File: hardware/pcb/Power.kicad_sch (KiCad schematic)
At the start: 12 parts, among them J2 USB_B_Micro, SW1 CSS-1210TB, U1 XC6808A4D28R-G, U3 NCP160AMX330TBG, U5 RN4989

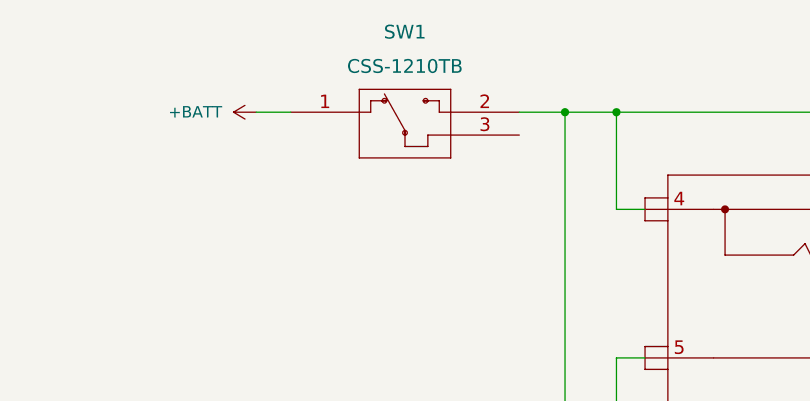
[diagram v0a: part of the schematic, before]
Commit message: Bump KiCad version to 7
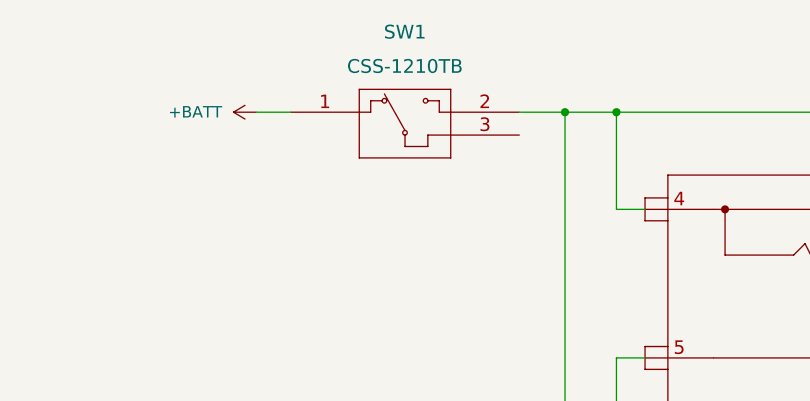
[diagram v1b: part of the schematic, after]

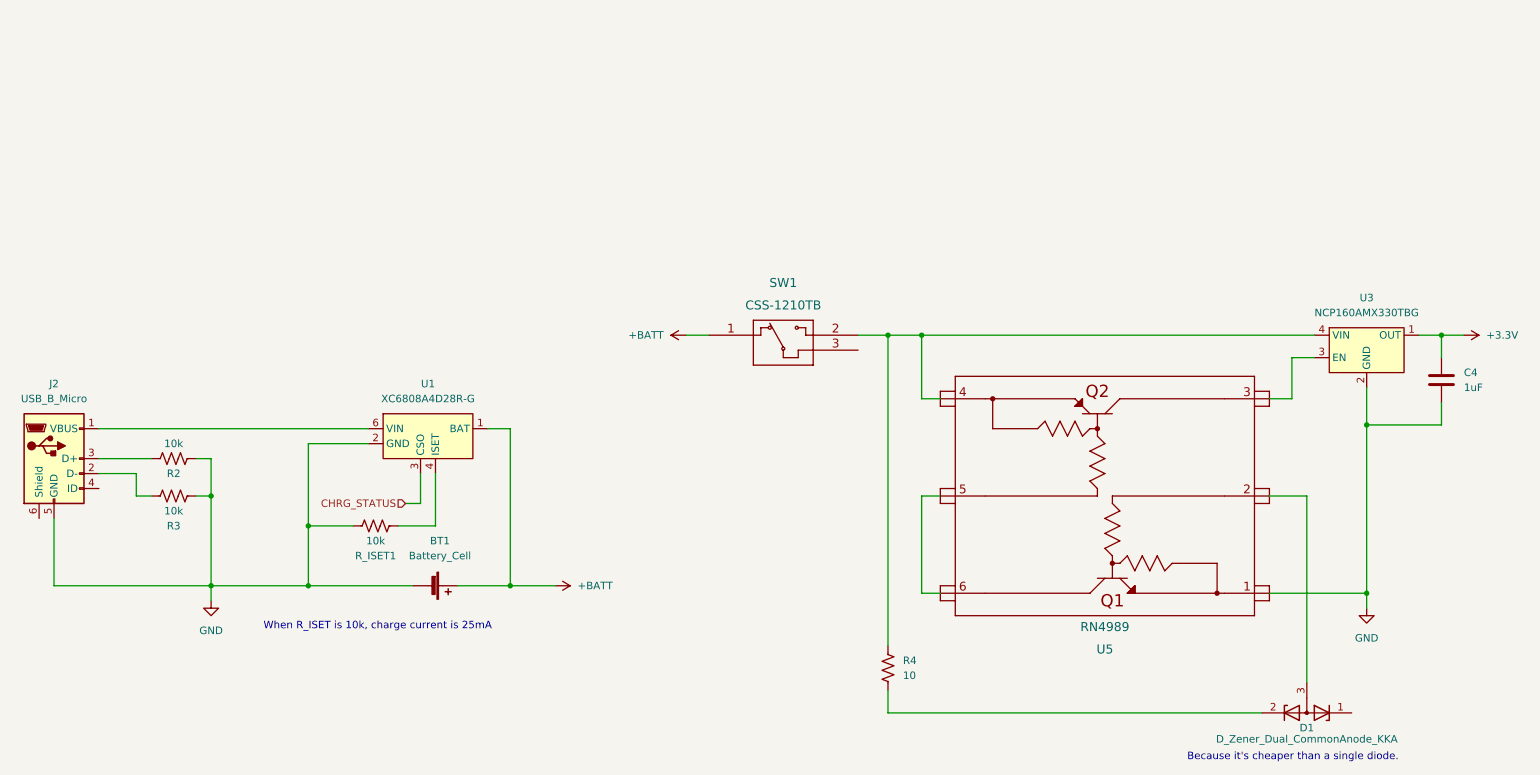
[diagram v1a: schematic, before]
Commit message: Replace XC6808 with MCP73831 in schematic
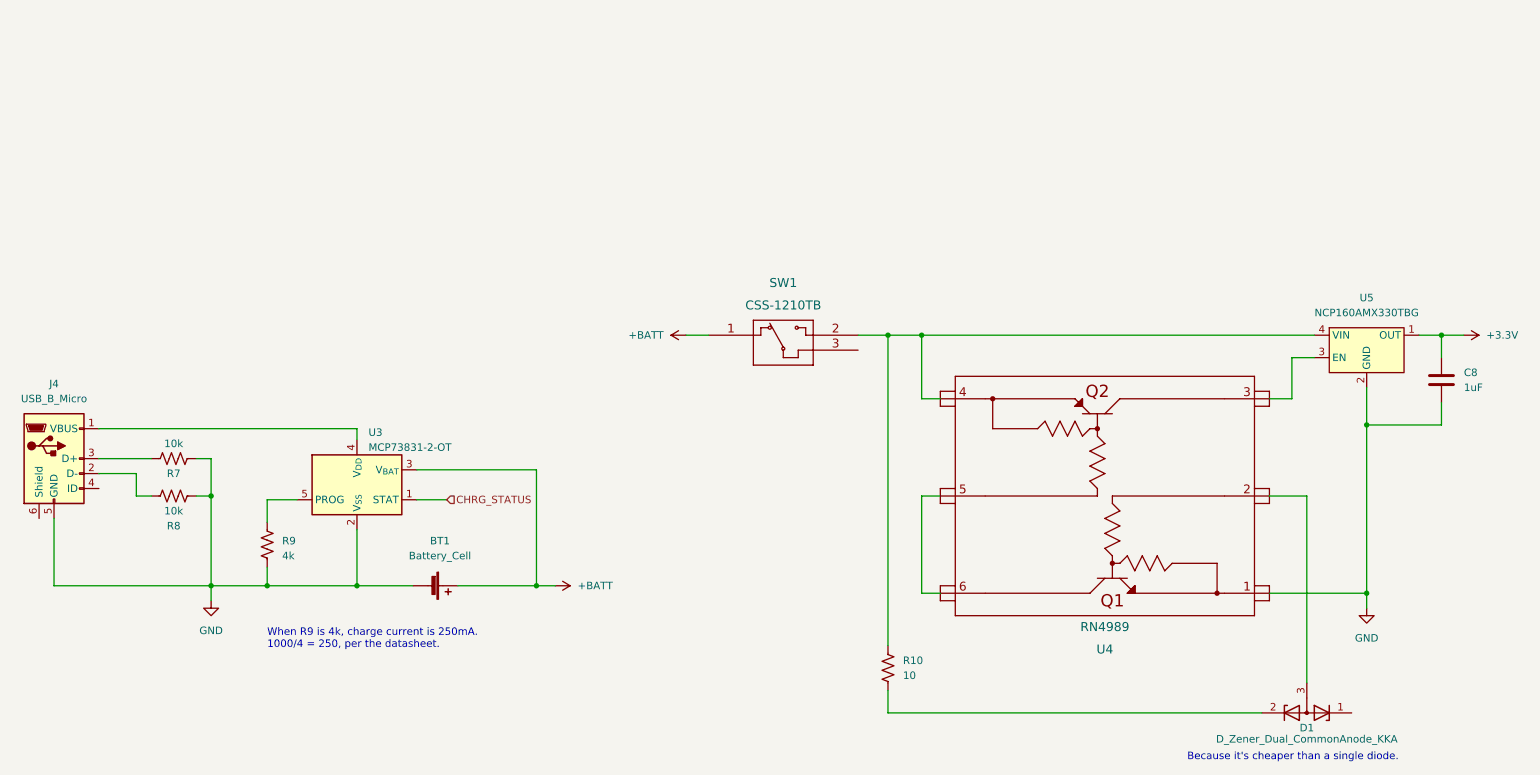
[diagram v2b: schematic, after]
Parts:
- removed R_ISET1: 10k, Resistor_SMD:R_1206_3216Metric_Pad1.30x1.75mm_HandSolder, symbol Device:R_US
- removed U1: XC6808A4D28R-G, Torex:USP-6B07, symbol Torex:XC6808A4D28R-G
- added R9: 4k, symbol Device:R_US
- added U3: MCP73831-2-OT, Package_TO_SOT_SMD:SOT-23-5, symbol Battery_Management:MCP73831-2-OT
- renumbered C4 to C8, J2 to J4, R4 to R10, R2 to R7, R3 to R8, U5 to U4, U3 to U5
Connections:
- net +BATT: now also U3.3 (V_{BAT})
- net CHRG_STATUS: now also U3.1 (STAT)
- net GND: now also R9.2, U3.2 (V_{SS})
- net at J4.1 (VBUS): now also U3.4 (V_{DD})
- new net: R9.1, U3.5 (PROG)
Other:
- note added: "When R9 is 4k, charge current is 250mA. 1000/4 = 250, per the datasheet."
- note removed: "When R_ISET is 10k, charge current is 25mA"

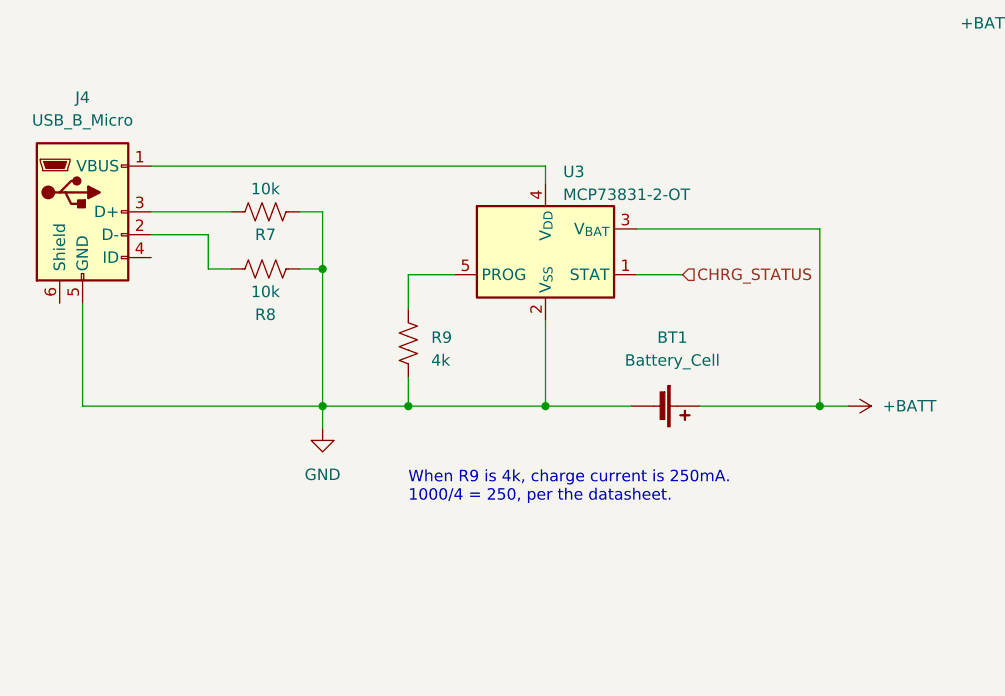
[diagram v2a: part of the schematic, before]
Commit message: Add MCP73831 to PCB
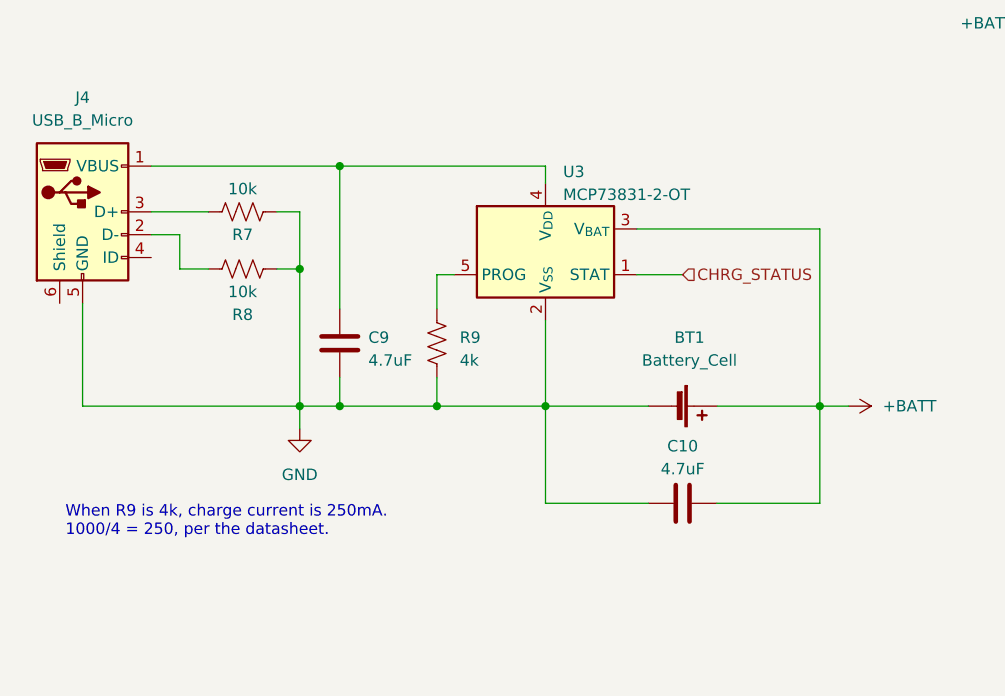
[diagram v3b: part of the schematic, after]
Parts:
- added C10, C9: 4.7uF, Capacitor_SMD:C_1206_3216Metric_Pad1.33x1.80mm_HandSolder, symbol Device:C
- R9: footprint (none) -> Resistor_SMD:R_1206_3216Metric_Pad1.30x1.75mm_HandSolder
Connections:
- net +BATT: now also C10.1
- net GND: now also C10.2, C9.2
- net at J4.1 (VBUS), U3.4 (V_{DD}): now also C9.1
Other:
- moved on the sheet: BT1, R7, R8, R9

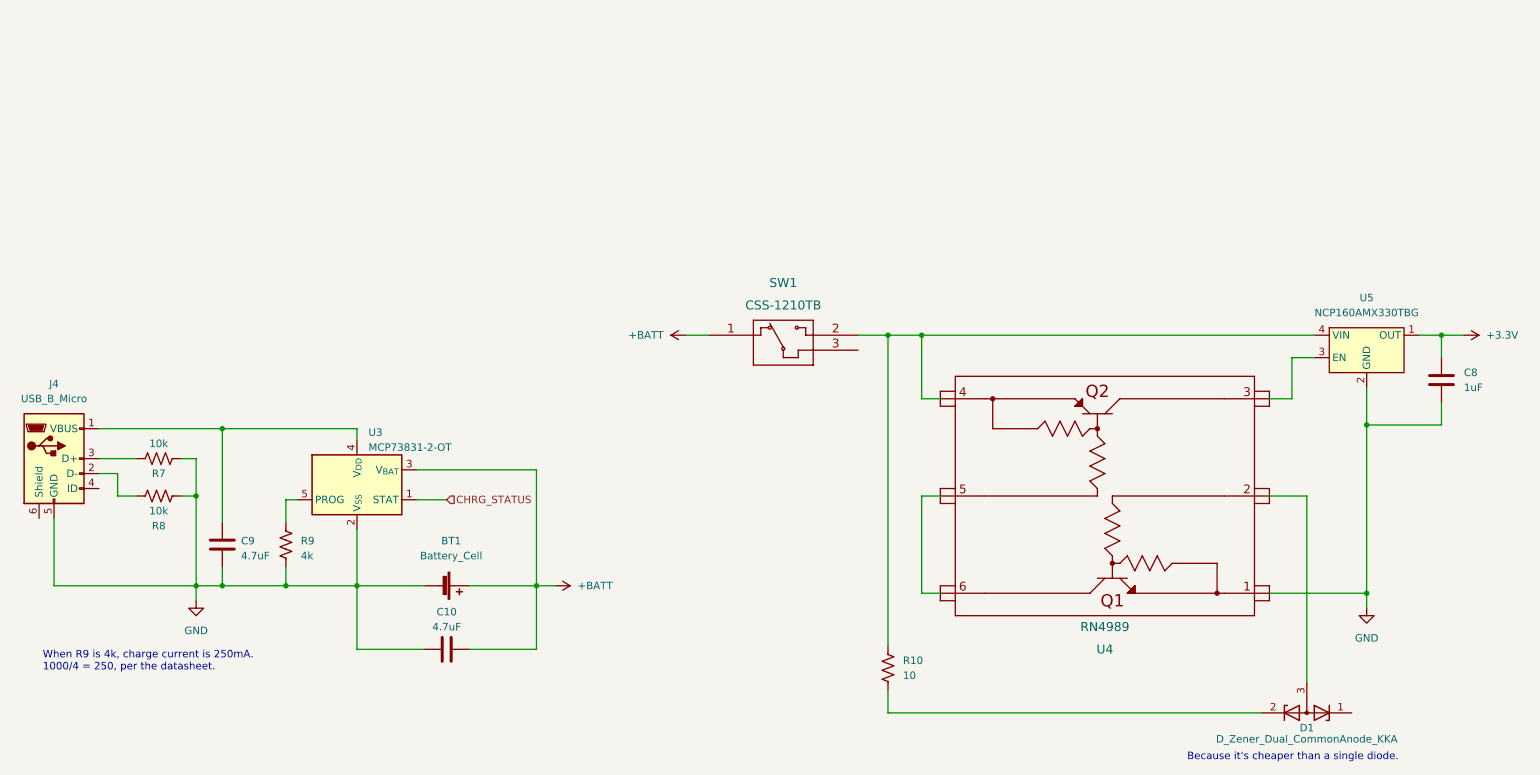
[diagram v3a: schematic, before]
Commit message: Use single resistor for setting amplifier gain
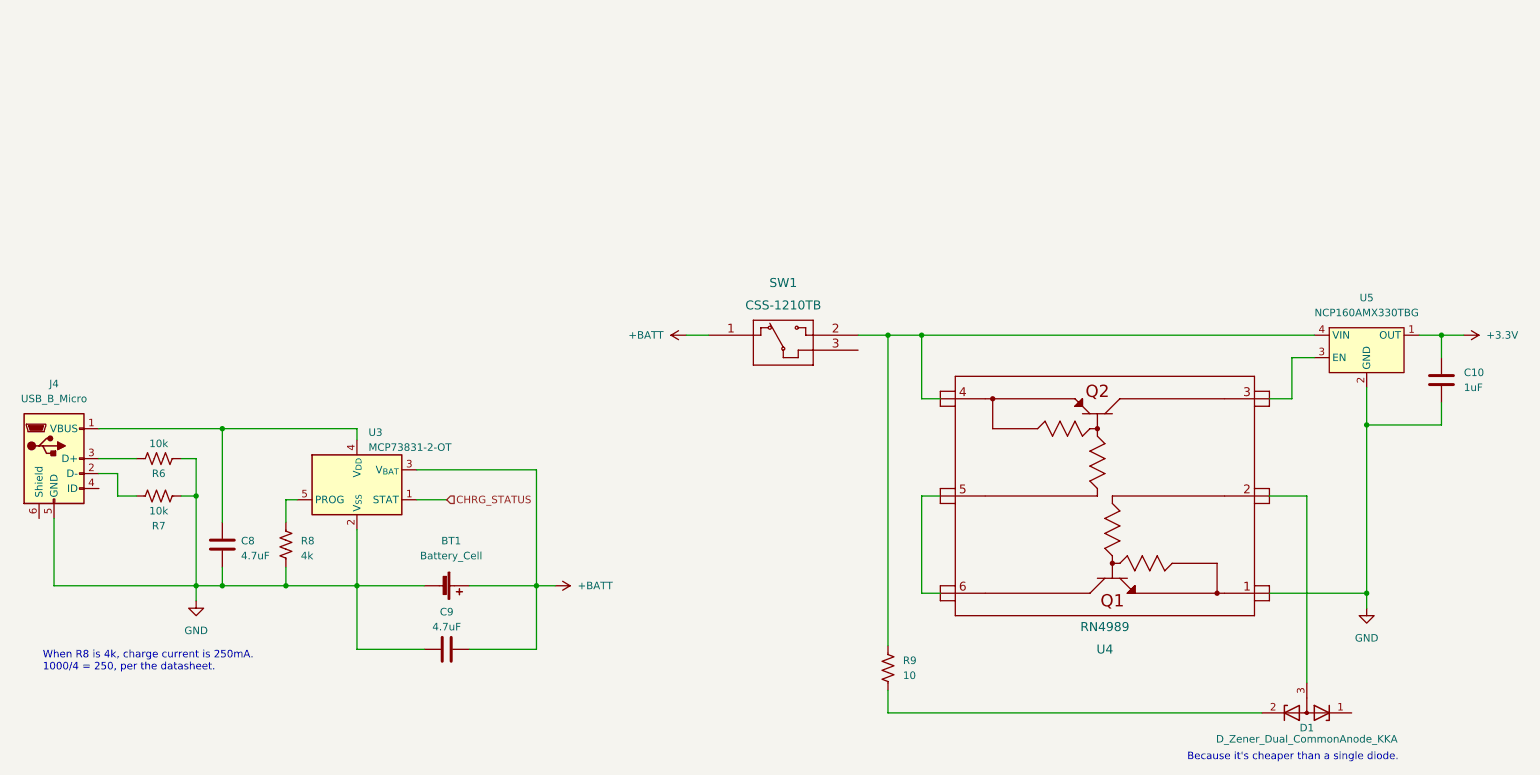
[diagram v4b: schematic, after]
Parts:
- renumbered C8 to C10, C9 to C8, C10 to C9, R7 to R6, R8 to R7, R9 to R8, R10 to R9
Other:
- note added: "When R8 is 4k, charge current is 250mA. 1000/4 = 250, per the datasheet."
- note removed: "When R9 is 4k, charge current is 250mA. 1000/4 = 250, per the datasheet."
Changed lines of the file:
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@@
     (effects (font (size 1.27 1.27)) (justify left bottom))
   )
-  (text "When R9 is 4k, charge current is 250mA.\n1000/4 = 250, per the datasheet."
+  (text "When R8 is 4k, charge current is 250mA.\n1000/4 = 250, per the datasheet."
     (at 22.86 128.27 0)
     (effects (font (size 1.27 1.27)) (justify left bottom))
@@
   (symbol (lib_id "power:GND") (at 247.65 117.475 0) (unit 1)
     (in_bom yes) (on_board yes) (dnp no) (fields_autoplaced)
-    (property "Reference" "#PWR019" (at 247.65 123.825 0)
+    (property "Reference" "#PWR018" (at 247.65 123.825 0)
       (effects (font (size 1.27 1.27)) hide)
     )
@@
       (project "Combadge"
         (path "/dc42e7bc-f663-434d-8744-232038ac4fdf/522738f4-f6b2-4897-a079-07da122bd152"
-          (reference "#PWR019") (unit 1)
+          (reference "#PWR018") (unit 1)
         )
       )
@@
   (symbol (lib_id "power:GND") (at 48.895 116.205 0) (unit 1)
     (in_bom yes) (on_board yes) (dnp no)
-    (property "Reference" "#PWR016" (at 48.895 122.555 0)
+    (property "Reference" "#PWR015" (at 48.895 122.555 0)
       (effects (font (size 1.27 1.27)) hide)
     )
@@
       (project "Combadge"
         (path "/dc42e7bc-f663-434d-8744-232038ac4fdf/522738f4-f6b2-4897-a079-07da122bd152"
-          (reference "#PWR016") (unit 1)
+          (reference "#PWR015") (unit 1)
         )
       )
@@
   (symbol (lib_id "power:+3.3V") (at 264.16 71.12 270) (unit 1)
     (in_bom yes) (on_board yes) (dnp no) (fields_autoplaced)
-    (property "Reference" "#PWR020" (at 260.35 71.12 0)
+    (property "Reference" "#PWR019" (at 260.35 71.12 0)
       (effects (font (size 1.27 1.27)) hide)
     )
@@
       (project "Combadge"
         (path "/dc42e7bc-f663-434d-8744-232038ac4fdf/522738f4-f6b2-4897-a079-07da122bd152"
-          (reference "#PWR020") (unit 1)
+          (reference "#PWR019") (unit 1)
         )
       )
@@
   (symbol (lib_id "Device:R_US") (at 64.135 106.68 0) (unit 1)
     (in_bom yes) (on_board yes) (dnp no) (fields_autoplaced)
-    (property "Reference" "R9" (at 66.675 106.045 0)
+    (property "Reference" "R8" (at 66.675 106.045 0)
       (effects (font (size 1.27 1.27)) (justify left))
     )
@@
       (project "Combadge"
         (path "/dc42e7bc-f663-434d-8744-232038ac4fdf/522738f4-f6b2-4897-a079-07da122bd152"
-          (reference "R9") (unit 1)
+          (reference "R8") (unit 1)
         )
       )
@@
   (symbol (lib_id "Device:C") (at 53.34 106.68 0) (unit 1)
     (in_bom yes) (on_board yes) (dnp no) (fields_autoplaced)
-    (property "Reference" "C9" (at 56.515 106.045 0)
+    (property "Reference" "C8" (at 56.515 106.045 0)
       (effects (font (size 1.27 1.27)) (justify left))
     )
@@
       (project "Combadge"
         (path "/dc42e7bc-f663-434d-8744-232038ac4fdf/522738f4-f6b2-4897-a079-07da122bd152"
-          (reference "C9") (unit 1)
+          (reference "C8") (unit 1)
         )
       )
@@
   (symbol (lib_id "Device:C") (at 91.44 124.46 270) (unit 1)
     (in_bom yes) (on_board yes) (dnp no) (fields_autoplaced)
-    (property "Reference" "C10" (at 91.44 118.11 90)
+    (property "Reference" "C9" (at 91.44 118.11 90)
       (effects (font (size 1.27 1.27)))
     )
@@
       (project "Combadge"
         (path "/dc42e7bc-f663-434d-8744-232038ac4fdf/522738f4-f6b2-4897-a079-07da122bd152"
-          (reference "C10") (unit 1)
+          (reference "C9") (unit 1)
         )
       )
@@
   (symbol (lib_id "Device:R_US") (at 42.545 92.075 90) (unit 1)
     (in_bom yes) (on_board yes) (dnp no)
-    (property "Reference" "R7" (at 42.545 94.615 90)
+    (property "Reference" "R6" (at 42.545 94.615 90)
       (effects (font (size 1.27 1.27)))
     )
@@
       (project "Combadge"
         (path "/dc42e7bc-f663-434d-8744-232038ac4fdf/522738f4-f6b2-4897-a079-07da122bd152"
-          (reference "R7") (unit 1)
+          (reference "R6") (unit 1)
         )
       )
@@
   (symbol (lib_id "power:+BATT") (at 132.08 71.12 90) (unit 1)
     (in_bom yes) (on_board yes) (dnp no)
-    (property "Reference" "#PWR018" (at 135.89 71.12 0)
+    (property "Reference" "#PWR017" (at 135.89 71.12 0)
       (effects (font (size 1.27 1.27)) hide)
     )
@@
       (project "Combadge"
         (path "/dc42e7bc-f663-434d-8744-232038ac4fdf/522738f4-f6b2-4897-a079-07da122bd152"
-          (reference "#PWR018") (unit 1)
+          (reference "#PWR017") (unit 1)
         )
       )
@@
   (symbol (lib_id "Device:R_US") (at 166.37 127.635 0) (unit 1)
     (in_bom yes) (on_board yes) (dnp no)
-    (property "Reference" "R10" (at 168.91 126.3649 0)
+    (property "Reference" "R9" (at 168.91 126.3649 0)
       (effects (font (size 1.27 1.27)) (justify left))
     )
@@
       (project "Combadge"
         (path "/dc42e7bc-f663-434d-8744-232038ac4fdf/522738f4-f6b2-4897-a079-07da122bd152"
-          (reference "R10") (unit 1)
+          (reference "R9") (unit 1)
         )
       )
@@
   (symbol (lib_id "power:+BATT") (at 109.855 113.665 270) (unit 1)
     (in_bom yes) (on_board yes) (dnp no) (fields_autoplaced)
-    (property "Reference" "#PWR017" (at 106.045 113.665 0)
+    (property "Reference" "#PWR016" (at 106.045 113.665 0)
       (effects (font (size 1.27 1.27)) hide)
     )
@@
       (project "Combadge"
         (path "/dc42e7bc-f663-434d-8744-232038ac4fdf/522738f4-f6b2-4897-a079-07da122bd152"
-          (reference "#PWR017") (unit 1)
+          (reference "#PWR016") (unit 1)
         )
       )
@@
   (symbol (lib_id "Device:C") (at 260.35 78.74 0) (unit 1)
     (in_bom yes) (on_board yes) (dnp no) (fields_autoplaced)
-    (property "Reference" "C8" (at 264.16 77.4699 0)
+    (property "Reference" "C10" (at 264.16 77.4699 0)
       (effects (font (size 1.27 1.27)) (justify left))
     )
@@
       (project "Combadge"
         (path "/dc42e7bc-f663-434d-8744-232038ac4fdf/522738f4-f6b2-4897-a079-07da122bd152"
-          (reference "C8") (unit 1)
+          (reference "C10") (unit 1)
         )
       )
@@
   (symbol (lib_id "Device:R_US") (at 42.545 98.425 90) (unit 1)
     (in_bom yes) (on_board yes) (dnp no)
-    (property "Reference" "R8" (at 42.545 103.505 90)
+    (property "Reference" "R7" (at 42.545 103.505 90)
       (effects (font (size 1.27 1.27)))
     )
@@
       (project "Combadge"
         (path "/dc42e7bc-f663-434d-8744-232038ac4fdf/522738f4-f6b2-4897-a079-07da122bd152"
-          (reference "R8") (unit 1)
-        )
-      )
+          (reference "R7") (unit 1)
+        )
+      )
